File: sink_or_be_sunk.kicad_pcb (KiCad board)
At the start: 2 copper layers, 90 x 100 mm, 49 parts, among them J1 Keypad_Conn, J2 Mux_Conn, J3 Display_Conn, J4 SWD_Conn, J5 Battery_Conn, J6 USB_B_Micro, M1 Motor_DC, Q1 IRLML5203, Q2 MMBT5550L, Q3 MMBT5550L, SW1 Reset_SW, U1 SN74HC151N, U2 LDL1117-SMD, U3 MCP73831-2-OT, U4 MCP608, U5 ESP32-WROOM-32, U6 CY7C65213A-28PVXI

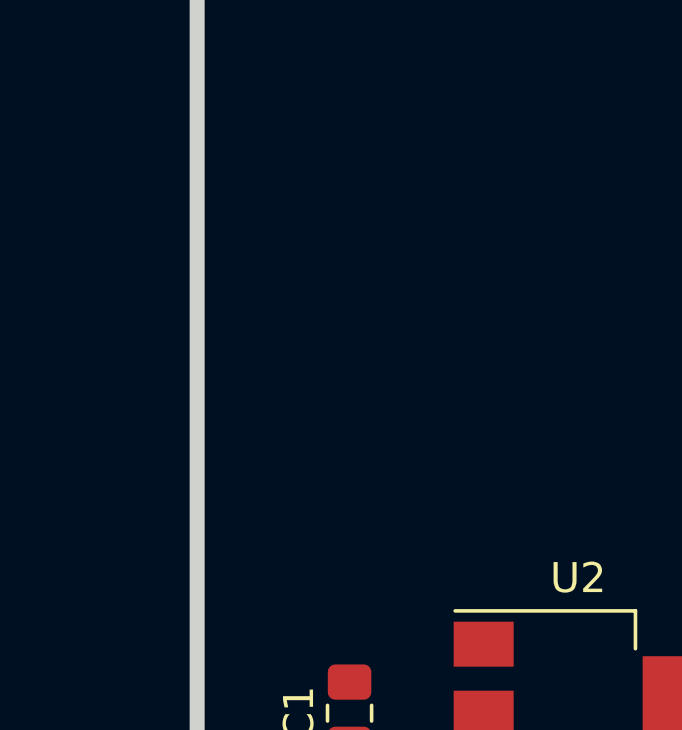
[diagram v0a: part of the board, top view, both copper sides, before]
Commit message: added electrical isoltion switch
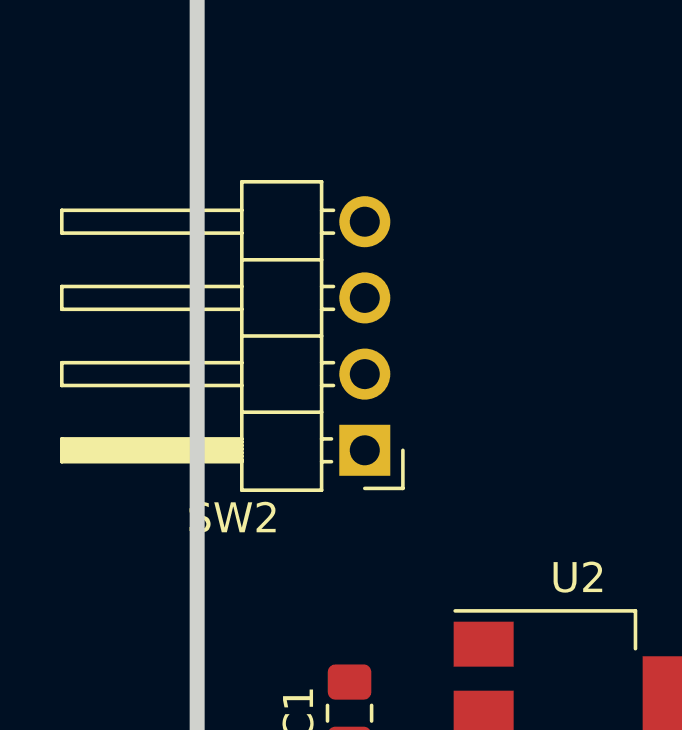
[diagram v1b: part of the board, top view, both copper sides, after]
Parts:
- added SW2: SW_DPST, Connector_PinHeader_2.54mm:PinHeader_1x04_P2.54mm_Horizontal, F.Cu at (194.8, 45.8)
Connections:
- J5 pad 1: +BATT -> Net-(J5-Pad1)
- J5 pad 2: GND -> Net-(J5-Pad2)

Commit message: redo of layout and minor circuit updates
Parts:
- added C12: 10uF, Capacitor_THT:CP_Radial_D8.0mm_P3.50mm, F.Cu at (429.3, 29.2)
- C7: footprint Capacitor_SMD:C_0805_2012Metric_Pad1.15x1.40mm_HandSolder -> Capacitor_THT:CP_Radial_D8.0mm_P3.50mm
- D2: value D_Zener -> D; footprint Diode_SMD:D_0805_2012Metric_Pad1.15x1.40mm_HandSolder -> Diode_THT:D_DO-15_P10.16mm_Horizontal
- J4: value SWD_Conn -> JTAG_Conn; footprint Connector_PinHeader_2.54mm:PinHeader_1x06_P2.54mm_Vertical -> Connector_PinHeader_2.54mm:PinHeader_1x04_P2.54mm_Vertical
- U1: footprint PCB_ESP32:SN74HC151N-PDIP -> Package_DIP:DIP-16_W10.16mm
- moved SW2 221.4 mm to (415.3, 66.0), turned to 0 degrees
- moved J6 220.9 mm to (414.0, 86.4), turned to 90 degrees
- moved Q1 201.3 mm to (415.3, 16.5)
- moved D2 196.1 mm to (403.9, 24.1), turned to 0 degrees
- moved M1 191.6 mm to (400.1, 14.0)
- moved J1 174.2 mm to (360.7, 11.4)
- moved R1 168.4 mm to (360.2, 17.3)
- moved R3 168.4 mm to (365.3, 17.3)
- moved R2 168.4 mm to (362.7, 17.3)
- moved R4 168.4 mm to (367.8, 17.3)
- moved U5 166.8 mm to (375.9, 110.5), turned to 180 degrees
- moved J4 156.7 mm to (416.6, 102.9), turned to 180 degrees
- moved R5 155.0 mm to (349.2, 38.1)
- moved R6 155.0 mm to (349.2, 33.0)
- moved C4 152.9 mm to (330.2, 35.6)
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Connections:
- J4 pad 1: /SCS_CMD -> /MTMS
- J4 pad 2: /SCK_CLK -> /MTDI
- J4 pad 3: /SWP_SD3 -> /MTCK
- J4 pad 4: /SHD_SD2 -> /MTDO
- LS1 pad 1: Net-(LS1-Pad1) -> Net-(C12-Pad1)
- RV1 pad 2: Net-(LS1-Pad1) -> Net-(C12-Pad2)
- U5 pad 13: /LCD_SCLK -> /MTMS
- U5 pad 14: /LED_OUT -> /MTDI
- U5 pad 16: /LCD_MOSI -> /MTCK
- U5 pad 17: /SHD_SD2 -> Net-(U5-Pad17)
- U5 pad 18: /SWP_SD3 -> Net-(U5-Pad18)
- U5 pad 19: /SCS_CMD -> /LCD_CS
- U5 pad 20: /SCK_CLK -> /LCD_SCLK
- U5 pad 21: /SDO_SD0 -> /LCD_MOSI
- U5 pad 22: /SDI_SD1 -> /LED_OUT
- U5 pad 23: /LCD_CS -> /MTDO

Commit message: minor updates to board settings
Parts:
- moved R11 11.6 mm to (412.3, 114.3)
- moved SW1 6.06 mm to (416.5, 112.6)
- moved C11 5.03 mm to (408.9, 114.3)
- moved J4 3.87 mm to (417.0, 106.7)
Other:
- net class Power: trace_width 0.5 -> 0.8128

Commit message: 10/7 organizing ratsnest more
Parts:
- removed D3, D4: LED, LED_THT:LED_D3.0mm
- removed R10, R9: 1k, Resistor_SMD:R_0805_2012Metric_Pad1.15x1.40mm_HandSolder
- added D5: D, Diode_THT:D_DO-15_P10.16mm_Horizontal, F.Cu at (300.9, 68.1)
- added J7: JTAG_Conn, Connector_PinHeader_2.54mm:PinHeader_1x02_P2.54mm_Vertical, F.Cu at (399.0, 40.4)
- added Q4: Q_PMOS_DGS, Package_TO_SOT_THT:TO-220-3_Vertical, F.Cu at (301.1, 79.8)
- added R12: 100k, Resistor_SMD:R_0805_2012Metric_Pad1.15x1.40mm_HandSolder, F.Cu at (318.6, 71.9)
- added TP1: TestPoint, TestPoint:TestPoint_Pad_2.0x2.0mm, F.Cu at (402.5, 93.3)
- added TP2: TestPoint, TestPoint:TestPoint_Pad_2.0x2.0mm, F.Cu at (399.0, 93.3)
- J3: footprint Connector_PinHeader_2.54mm:PinHeader_1x05_P2.54mm_Horizontal -> Connector_PinHeader_2.54mm:PinHeader_1x05_P2.54mm_Vertical
- LS1, SW1: footprint Connector_PinHeader_2.54mm:PinHeader_1x02_P2.54mm_Horizontal -> Connector_PinHeader_2.54mm:PinHeader_1x02_P2.54mm_Vertical
- Q1: footprint Package_TO_SOT_SMD:SOT-23 -> Package_TO_SOT_THT:TO-220-3_Vertical
- Q2, Q3: value MMBT5550L -> 2N3704; footprint Package_TO_SOT_SMD:SOT-23 -> Package_TO_SOT_THT:TO-92
- RV1: footprint Connector_PinHeader_2.54mm:PinHeader_1x03_P2.54mm_Horizontal -> Connector_PinHeader_2.54mm:PinHeader_1x03_P2.54mm_Vertical
- SW2: footprint Connector_PinHeader_2.54mm:PinHeader_1x04_P2.54mm_Horizontal -> Connector_PinHeader_2.54mm:PinHeader_1x04_P2.54mm_Vertical
- moved J5 108.7 mm to (401.3, 83.6)
- moved C8 81.5 mm to (402.6, 100.6), turned to 270 degrees
- moved C5 77.7 mm to (396.2, 100.5), turned to 0 degrees
- moved C10 77.5 mm to (396.2, 98.3), turned to 0 degrees
- moved J4 76.2 mm to (398.8, 32.7)
- moved R11 65.9 mm to (395.7, 50.5)
- moved SW1 65.6 mm to (400.5, 49.0)
- moved U5 64.0 mm to (376.5, 46.5)
- moved C11 63.4 mm to (392.1, 53.2), turned to 270 degrees
- moved U6 63.1 mm to (389.4, 98.8), turned to 0 degrees
- moved D2 61.7 mm to (342.3, 29.1)
- moved C6 58.8 mm to (387.7, 54.0), turned to 270 degrees
- moved Q1 58.0 mm to (357.7, 23.1)
- moved M1 56.3 mm to (344.6, 23.3), turned to 180 degrees
- moved C2 56.0 mm to (323.5, 74.4), turned to 180 degrees
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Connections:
- net Net-(C5-Pad1) renamed /VCCD4
- J1 pad 1: Net-(J1-Pad1) -> /KEYPAD_COL0
- J1 pad 2: Net-(J1-Pad2) -> /KEYPAD_COL1
- J1 pad 3: Net-(J1-Pad3) -> /KEYPAD_COL2
- J1 pad 4: Net-(J1-Pad4) -> /KEYPAD_COL3
- J1 pad 5: /KEYPAD_COL0 -> Net-(J1-Pad5)
- J1 pad 6: /KEYPAD_COL1 -> Net-(J1-Pad6)
- J1 pad 7: /KEYPAD_COL2 -> Net-(J1-Pad7)
- J1 pad 8: /KEYPAD_COL3 -> Net-(J1-Pad8)
- J2 pad 1: /MUX_ROW0 -> /MUX_ROW3
- J2 pad 2: /MUX_ROW1 -> /MUX_ROW2
- J2 pad 3: /MUX_ROW2 -> /MUX_ROW1
- J2 pad 4: /MUX_ROW3 -> /MUX_ROW0
- J3 pad 2: /LCD_SCLK -> /LCD_MOSI
- J3 pad 3: /LCD_MOSI -> /LCD_SCLK
- Q2 pad 1: Net-(Q2-Pad1) -> /DTR
- Q2 pad 2: /DTR -> /GPIO0
- Q2 pad 3: /GPIO0 -> Net-(Q2-Pad3)
- Q3 pad 1: Net-(Q3-Pad1) -> /RTS
- Q3 pad 2: /RTS -> /RESET
- Q3 pad 3: /RESET -> Net-(Q3-Pad3)
- R1 pad 1: Net-(J1-Pad1) -> Net-(J1-Pad5)
- R2 pad 1: Net-(J1-Pad2) -> Net-(J1-Pad6)
- R3 pad 1: Net-(J1-Pad3) -> Net-(J1-Pad7)
- R4 pad 1: Net-(J1-Pad4) -> Net-(J1-Pad8)
- R7 pad 1: Net-(Q2-Pad1) -> Net-(Q2-Pad3)
- R8 pad 1: Net-(Q3-Pad1) -> Net-(Q3-Pad3)
- SW2 pad 2: Net-(J5-Pad2) -> Net-(J5-Pad1)
- SW2 pad 4: Net-(J5-Pad1) -> Net-(J5-Pad2)
- U2 pad 3: VBUS -> Net-(D5-Pad1)
- U5 pad 11: /KEYPAD_COL0 -> /KEYPAD_ROW1
- U5 pad 12: /KEYPAD_COL1 -> /KEYPAD_ROW0
- U5 pad 17: Net-(U5-Pad17) -> /KEYPAD_COL3
- U5 pad 18: Net-(U5-Pad18) -> /KEYPAD_COL2
- U5 pad 22: /LED_OUT -> /KEYPAD_COL1
- U5 pad 24: /MUX_COL_SEL0 -> /KEYPAD_COL0
- U5 pad 26: /MUX_COL_SEL1 -> /MOTOR
- U5 pad 27: /KEYPAD_ROW0 -> BOAT_INPUT
- U5 pad 28: /KEYPAD_ROW1 -> /MUX_COL_SEL2
- U5 pad 29: /MUX_COL_SEL2 -> /MUX_COL_SEL1
- U5 pad 30: /KEYPAD_ROW2 -> /MUX_COL_SEL0
- U5 pad 31: /KEYPAD_ROW3 -> /MUX_ROW_SEL0
- U5 pad 33: /MUX_ROW_SEL0 -> /MUX_ROW_SEL1
- U5 pad 36: /MUX_ROW_SEL1 -> /MUX_ROW_SEL2
- U5 pad 37: /MUX_ROW_SEL2 -> /LED_OUT
- U5 pad 6: BOAT_INPUT -> /DBG1
- U5 pad 7: /MOTOR -> /DBG2
- U5 pad 8: /KEYPAD_COL2 -> /KEYPAD_ROW3
- U5 pad 9: /KEYPAD_COL3 -> /KEYPAD_ROW2

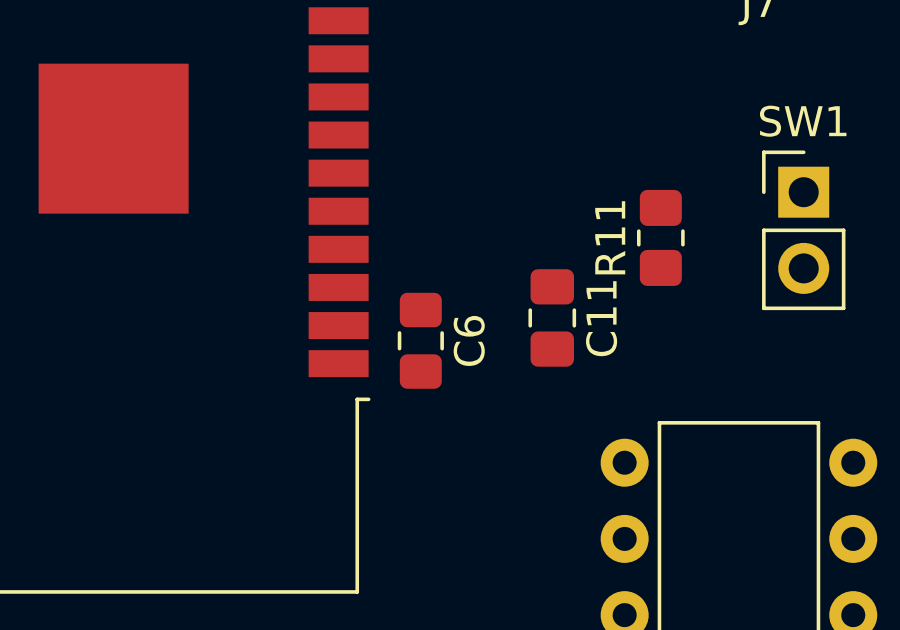
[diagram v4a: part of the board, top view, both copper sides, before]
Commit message: updated with todos from talk with prof
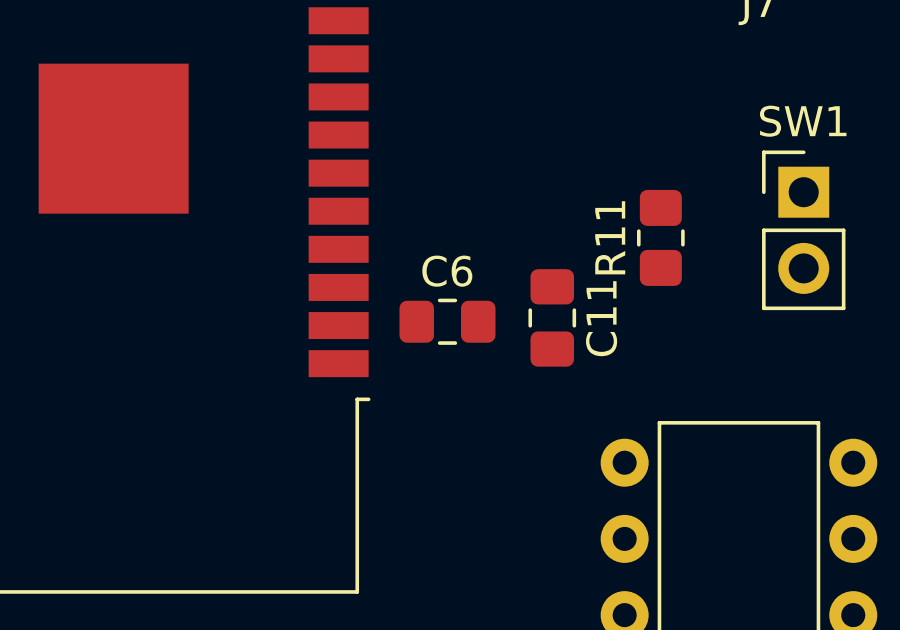
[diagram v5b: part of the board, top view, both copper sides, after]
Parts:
- moved C6 1.09 mm to (388.6, 53.3), turned to 0 degrees

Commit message: finished routing power and programming circuit
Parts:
- added D3: LED, LED_THT:LED_D3.0mm, F.Cu at (419.7, -46.0)
- added H5: Mounting, MountingHole:MountingHole_3.2mm_M3, F.Cu at (425.7, -26.2)
- added J10: Grid_Conn, Connector_PinSocket_2.54mm:PinSocket_1x06_P2.54mm_Vertical, F.Cu at (364.9, 6.48)
- added J11: Grid_Conn, Connector_PinSocket_2.54mm:PinSocket_1x06_P2.54mm_Vertical, F.Cu at (361.2, 6.48)
- added J12: Grid_Conn, Connector_PinSocket_2.54mm:PinSocket_1x06_P2.54mm_Vertical, F.Cu at (372.2, -11.6)
- added J13: Grid_Conn, Connector_PinSocket_2.54mm:PinSocket_1x06_P2.54mm_Vertical, F.Cu at (368.6, -11.6)
- added J14: Grid_Conn, Connector_PinSocket_2.54mm:PinSocket_1x06_P2.54mm_Vertical, F.Cu at (364.9, -11.6)
- added J15: Grid_Conn, Connector_PinSocket_2.54mm:PinSocket_1x06_P2.54mm_Vertical, F.Cu at (361.2, -11.6)
- added J16: Grid_Conn, Connector_PinSocket_2.54mm:PinSocket_1x06_P2.54mm_Vertical, F.Cu at (372.2, -29.6)
- added J17: Grid_Conn, Connector_PinSocket_2.54mm:PinSocket_1x06_P2.54mm_Vertical, F.Cu at (361.2, -29.6)
- added J18: Grid_Conn, Connector_PinSocket_2.54mm:PinSocket_1x06_P2.54mm_Vertical, F.Cu at (364.9, -29.6)
- added J19: Grid_Conn, Connector_PinSocket_2.54mm:PinSocket_1x06_P2.54mm_Vertical, F.Cu at (368.6, -29.6)
- added J20: Grid_Conn, Connector_PinSocket_2.54mm:PinSocket_1x06_P2.54mm_Vertical, F.Cu at (372.1, -47.8)
- added J21: Grid_Conn, Connector_PinSocket_2.54mm:PinSocket_1x06_P2.54mm_Vertical, F.Cu at (368.4, -47.8)
- added J22: Grid_Conn, Connector_PinSocket_2.54mm:PinSocket_1x06_P2.54mm_Vertical, F.Cu at (364.7, -47.8)
- added J23: Grid_Conn, Connector_PinSocket_2.54mm:PinSocket_1x06_P2.54mm_Vertical, F.Cu at (361.1, -47.8)
- added J8: Grid_Conn_LED, Connector_PinSocket_2.54mm:PinSocket_1x07_P2.54mm_Vertical, F.Cu at (372.2, 6.48)
- added J9: Grid_Conn, Connector_PinSocket_2.54mm:PinSocket_1x06_P2.54mm_Vertical, F.Cu at (368.6, 6.48)
- added R10: 20, Resistor_SMD:R_0805_2012Metric_Pad1.20x1.40mm_HandSolder, F.Cu at (331.1, 39.2)
- added R13: 470, Resistor_SMD:R_0805_2012Metric_Pad1.20x1.40mm_HandSolder, F.Cu at (442.7, -41.0)
- added R14: 20, Resistor_SMD:R_0805_2012Metric_Pad1.20x1.40mm_HandSolder, F.Cu at (331.0, 42.3)
- added R15: 20, Resistor_SMD:R_0805_2012Metric_Pad1.20x1.40mm_HandSolder, F.Cu at (330.8, 44.5)
- added R16: 20, Resistor_SMD:R_0805_2012Metric_Pad1.20x1.40mm_HandSolder, F.Cu at (330.5, 46.7)
- added R17: 20, Resistor_SMD:R_0805_2012Metric_Pad1.20x1.40mm_HandSolder, F.Cu at (331.1, 50.4)
- added R18: 20, Resistor_SMD:R_0805_2012Metric_Pad1.20x1.40mm_HandSolder, F.Cu at (331.1, 52.3)
- added R19: 20, Resistor_SMD:R_0805_2012Metric_Pad1.20x1.40mm_HandSolder, F.Cu at (421.8, 16.9)
- added R20: 20, Resistor_SMD:R_0805_2012Metric_Pad1.20x1.40mm_HandSolder, F.Cu at (419.2, 17.3)
- added R21: 20, Resistor_SMD:R_0805_2012Metric_Pad1.20x1.40mm_HandSolder, F.Cu at (416.6, 17.1)
- added R22: 20, Resistor_SMD:R_0805_2012Metric_Pad1.20x1.40mm_HandSolder, F.Cu at (493.1, 77.6)
- added R23: 20, Resistor_SMD:R_0805_2012Metric_Pad1.20x1.40mm_HandSolder, F.Cu at (331.0, 54.7)
- added R24: 20, Resistor_SMD:R_0805_2012Metric_Pad1.20x1.40mm_HandSolder, F.Cu at (494.2, 79.8)
- added R25: 20, Resistor_SMD:R_0805_2012Metric_Pad1.20x1.40mm_HandSolder, F.Cu at (494.2, 82.4)
- added R26: 20, Resistor_SMD:R_0805_2012Metric_Pad1.20x1.40mm_HandSolder, F.Cu at (494.4, 85.9)
- added R9: 20, Resistor_SMD:R_0805_2012Metric_Pad1.20x1.40mm_HandSolder, F.Cu at (331.0, 35.9)
- C1, C2, C3, C4: footprint Capacitor_SMD:C_0805_2012Metric_Pad1.18x1.45mm_HandSolder -> Capacitor_THT:CP_Radial_D4.0mm_P2.00mm
- C12: footprint Capacitor_THT:CP_Radial_D8.0mm_P3.50mm -> Capacitor_THT:CP_Radial_D4.0mm_P2.00mm
- C7: value 100uF -> 10uF; footprint Capacitor_THT:CP_Radial_D8.0mm_P3.50mm -> Capacitor_THT:CP_Radial_D4.0mm_P2.00mm
- D2, D5: footprint Diode_THT:D_DO-15_P10.16mm_Horizontal -> Diode_THT:D_A-405_P7.62mm_Horizontal
- H1, H3, H4: value MountingHole -> Mounting
- H2: value MountingHole -> ESP_GND_Pad_Hole; footprint MountingHole:MountingHole_3.2mm_M3 -> MountingHole:MountingHole_2.2mm_M2_DIN965_Pad
- J7: value JTAG_Conn -> Debug_Conn
- Q1: value IRLML5203 -> IRL530
- Q4: footprint Package_TO_SOT_THT:TO-220-3_Vertical -> Package_TO_SOT_THT:TO-220-3_Horizontal_TabDown
- TP1, TP2: footprint TestPoint:TestPoint_Pad_2.0x2.0mm -> TestPoint:TestPoint_Plated_Hole_D2.0mm
- moved H3 273.6 mm to (426.8, -38.5)
- moved H1 272.6 mm to (464.7, -25.8)
- moved H4 215.7 mm to (438.8, -24.3)
- moved H2 174.7 mm to (414.3, 124.6)
- moved C2 167.9 mm to (482.2, 128.9), turned to 270 degrees
- moved D5 164.4 mm to (454.8, 125.7), turned to 180 degrees
- moved C1 161.0 mm to (475.9, 128.8), turned to 270 degrees
- moved U2 156.3 mm to (479.0, 122.4)
- moved Q4 155.4 mm to (452.4, 115.2), turned to 270 degrees
- moved R12 135.8 mm to (443.6, 125.0), turned to 180 degrees
- moved C4 129.5 mm to (446.7, 119.8), turned to 270 degrees
- moved C3 129.0 mm to (440.4, 119.8), turned to 270 degrees
- moved J4 115.0 mm to (501.1, 85.3)
- moved J7 108.8 mm to (436.2, 142.6), turned to 270 degrees
- moved D1 105.0 mm to (446.9, 113.0), turned to 0 degrees
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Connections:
- net /SENSOR_VN renamed Net-(U5-Pad5)
- net /SENSOR_VP renamed Net-(U5-Pad4)
- net BOAT_INPUT renamed /BOAT_INPUT
- C1 pad 1: VBUS -> /Vin
- D5 pad 1: Net-(D5-Pad1) -> /Vin
- H2 pad 1: (no net) -> GND
- J2 pad 1: /MUX_ROW3 -> Net-(J2-Pad1)
- J2 pad 2: /MUX_ROW2 -> Net-(J2-Pad2)
- J2 pad 3: /MUX_ROW1 -> Net-(J2-Pad3)
- J2 pad 4: /MUX_ROW0 -> Net-(J2-Pad4)
- J2 pad 5: /MUX_ROW4 -> Net-(J2-Pad5)
- J2 pad 6: /MUX_ROW5 -> Net-(J2-Pad6)
- J2 pad 7: /MUX_ROW6 -> Net-(J2-Pad7)
- J2 pad 8: /MUX_ROW7 -> Net-(J2-Pad8)
- J3 pad 2: /LCD_MOSI -> Net-(J3-Pad2)
- J3 pad 3: /LCD_SCLK -> Net-(J3-Pad3)
- J3 pad 4: /LCD_CS -> Net-(J3-Pad4)
- J4 pad 1: /MTMS -> Net-(J4-Pad1)
- J4 pad 2: /MTDI -> Net-(J4-Pad2)
- J4 pad 3: /MTCK -> Net-(J4-Pad3)
- J4 pad 4: /MTDO -> Net-(J4-Pad4)
- Q1 pad 2: GND -> Net-(D2-Pad2)
- Q1 pad 3: Net-(D2-Pad2) -> GND
- Q4 pad 3: Net-(D5-Pad1) -> /Vin
- SW2 pad 1: GND -> +BATT
- SW2 pad 2: Net-(J5-Pad1) -> Net-(J5-Pad2)
- SW2 pad 3: +BATT -> GND
- SW2 pad 4: Net-(J5-Pad2) -> Net-(J5-Pad1)
- U2 pad 3: Net-(D5-Pad1) -> /Vin
- U4 pad 2: /DAC_OUT -> /SPEAKER
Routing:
- net VBUS: track 0.00 -> 93.7 mm, vias 0 -> 2
- net /RXD0: track 0.00 -> 57.4 mm, vias 0 -> 2
- net /TXD0: track 0.00 -> 51.7 mm, vias 0 -> 2
- net GND: track 0.00 -> 45.0 mm, vias 0 -> 1
- net +BATT: track 0.00 -> 43.0 mm
- net Net-(J6-Pad2): track 0.00 -> 42.9 mm
- net Net-(J6-Pad3): track 0.00 -> 41.3 mm
- net /GPIO0: track 0.00 -> 35.6 mm, vias 0 -> 1
- net /Vin: track 0.00 -> 32.9 mm
- net /RTS: track 0.00 -> 32.1 mm, vias 0 -> 2
- net /DTR: track 0.00 -> 31.2 mm, vias 0 -> 2
- net +3V3: track 0.00 -> 30.6 mm, vias 0 -> 1
- net /RESET: track 0.00 -> 23.9 mm
- net Net-(J5-Pad2): track 0.00 -> 11.7 mm
- net Net-(D1-Pad1): track 0.00 -> 11.3 mm
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- added copper zone on B.Cu, net +3V3
- added copper zone on F.Cu, net +3V3
- added copper zone on B.Cu, net GND
- added copper zone on F.Cu, net GND
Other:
- board outline removed
- net class Small added: clearance 0.127, trace_width 0.254, via_dia 0.762, via_drill 0.381
